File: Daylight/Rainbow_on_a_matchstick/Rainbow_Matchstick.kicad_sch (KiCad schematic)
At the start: 22 parts, among them J1 Conn_01x03_Male, J2 Conn_01x01_Male, J3 Conn_01x01_Male

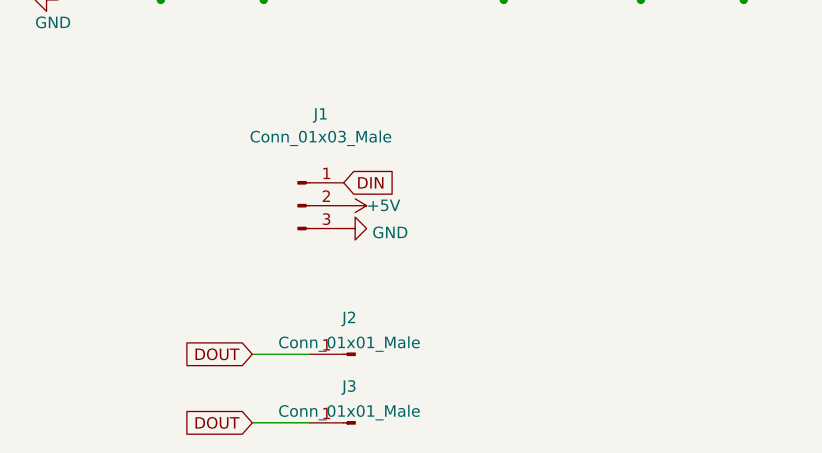
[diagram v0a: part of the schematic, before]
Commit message: Daylight | Add output connectors to the RGB sticks
Provided pick and place files for all varieties as well.
Created individual README.md files with BOM and changelog.
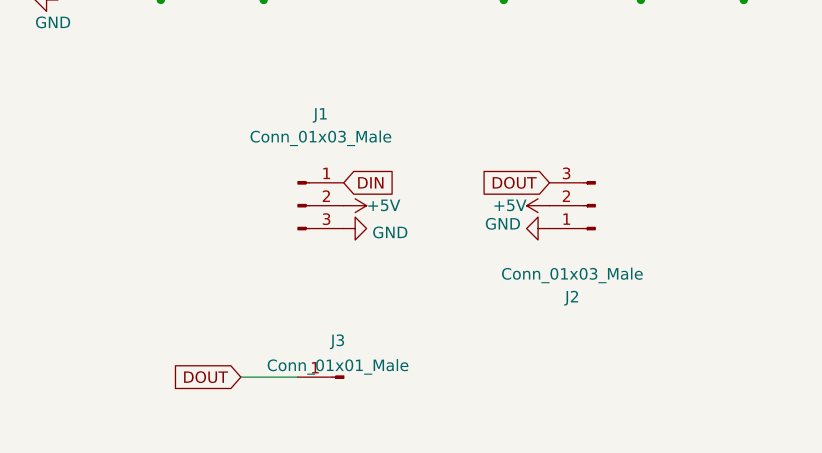
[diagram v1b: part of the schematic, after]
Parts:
- removed J2: Conn_01x01_Male, Daylight:PinHeader-1-with-SMDpad, symbol Connector:Conn_01x01_Male
- added J2: Conn_01x03_Male, Daylight:JST_XH_S3B-XH-A-1_1x03_P2.50mm_Horizontal, symbol Connector:Conn_01x03_Male
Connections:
- net +5V: now also J2.2 (Pin_2)
- net DOUT: now also J2.3 (Pin_3)
- net GND: now also J2.1 (Pin_1)
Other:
- moved on the sheet: J3
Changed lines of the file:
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@@
-    (stroke (width 0) (type default) (color 0 0 0 0))
-  )
-  (wire (pts (xy 48.26 105.41) (xy 54.61 105.41))
     (stroke (width 0) (type default) (color 0 0 0 0))
   )
@@
     (stroke (width 0) (type default) (color 0 0 0 0))
   )
-  (wire (pts (xy 48.26 113.03) (xy 54.61 113.03))
+  (wire (pts (xy 46.99 107.95) (xy 53.34 107.95))
     (stroke (width 0) (type default) (color 0 0 0 0))
   )
@@
     )
   )
+  (global_label "DOUT" (shape input) (at 81.28 86.36 180) (fields_autoplaced)
+    (effects (font (size 1.27 1.27)) (justify right))
+    (property "Intersheet References" "${INTERSHEET_REFS}" (id 0) (at 73.9683 86.2806 0)
+      (effects (font (size 1.27 1.27)) (justify right) hide)
+    )
+  )
   (global_label "DIN" (shape input) (at 26.67 35.56 180) (fields_autoplaced)
     (effects (font (size 1.27 1.27)) (justify right))
@@
     )
   )
-  (global_label "DOUT" (shape input) (at 48.26 113.03 180) (fields_autoplaced)
+  (global_label "DOUT" (shape input) (at 46.99 107.95 180) (fields_autoplaced)
     (effects (font (size 1.27 1.27)) (justify right))
-    (property "Intersheet References" "${INTERSHEET_REFS}" (id 0) (at 40.9483 112.9506 0)
-      (effects (font (size 1.27 1.27)) (justify right) hide)
-    )
-  )
-  (global_label "DOUT" (shape input) (at 48.26 105.41 180) (fields_autoplaced)
-    (effects (font (size 1.27 1.27)) (justify right))
-    (property "Intersheet References" "${INTERSHEET_REFS}" (id 0) (at 40.9483 105.3306 0)
+    (property "Intersheet References" "${INTERSHEET_REFS}" (id 0) (at 39.6783 107.8706 0)
       (effects (font (size 1.27 1.27)) (justify right) hide)
     )
@@
   (symbol (lib_id "power:GND") (at 58.42 91.44 90) (unit 1)
     (in_bom yes) (on_board yes) (fields_autoplaced)
-    (property "Reference" "#PWR08" (id 0) (at 64.77 91.44 0)
+    (property "Reference" "#PWR09" (id 0) (at 64.77 91.44 0)
       (effects (font (size 1.27 1.27)) hide)
     )
@@
     (pin "4")
   )
-  (symbol (lib_id "Connector:Conn_01x01_Male") (at 59.69 105.41 180) (unit 1)
-    (in_bom yes) (on_board yes) (fields_autoplaced)
-    (property "Reference" "J2" (id 0) (at 59.055 101.3673 0))
-    (property "Value" "Conn_01x01_Male" (id 1) (at 59.055 104.1424 0))
-    (property "Footprint" "Daylight:PinHeader-1-with-SMDpad" (id 2) (at 59.69 105.41 0)
-      (effects (font (size 1.27 1.27)) hide)
-    )
-    (property "Datasheet" "~" (id 3) (at 59.69 105.41 0)
-      (effects (font (size 1.27 1.27)) hide)
-    )
-    (pin "1")
-  )
   (symbol (lib_id "LED:WS2812B") (at 156.21 35.56 0) (unit 1)
     (in_bom yes) (on_board yes)
@@
     (pin "4")
   )
-  (symbol (lib_id "Connector:Conn_01x01_Male") (at 59.69 113.03 180) (unit 1)
-    (in_bom yes) (on_board yes) (fields_autoplaced)
-    (property "Reference" "J3" (id 0) (at 59.055 108.9873 0))
-    (property "Value" "Conn_01x01_Male" (id 1) (at 59.055 111.7624 0))
-    (property "Footprint" "Daylight:PinHeader-1-with-SMDpad" (id 2) (at 59.69 113.03 0)
-      (effects (font (size 1.27 1.27)) hide)
-    )
-    (property "Datasheet" "~" (id 3) (at 59.69 113.03 0)
+  (symbol (lib_id "Connector:Conn_01x01_Male") (at 58.42 107.95 180) (unit 1)
+    (in_bom yes) (on_board yes) (fields_autoplaced)
+    (property "Reference" "J3" (id 0) (at 57.785 103.9073 0))
+    (property "Value" "Conn_01x01_Male" (id 1) (at 57.785 106.6824 0))
+    (property "Footprint" "Daylight:PinHeader-1-with-SMDpad" (id 2) (at 58.42 107.95 0)
+      (effects (font (size 1.27 1.27)) hide)
+    )
+    (property "Datasheet" "~" (id 3) (at 58.42 107.95 0)
       (effects (font (size 1.27 1.27)) hide)
     )
@@
     (pin "1")
     (pin "2")
+  )
+  (symbol (lib_id "Connector:Conn_01x03_Male") (at 86.36 88.9 180) (unit 1)
+    (in_bom yes) (on_board yes)
+    (property "Reference" "J2" (id 0) (at 83.82 99.06 0))
+    (property "Value" "Conn_01x03_Male" (id 1) (at 83.82 96.52 0))
+    (property "Footprint" "Daylight:JST_XH_S3B-XH-A-1_1x03_P2.50mm_Horizontal" (id 2) (at 86.36 88.9 0)
+      (effects (font (size 1.27 1.27)) hide)
+    )
+    (property "Datasheet" "~" (id 3) (at 86.36 88.9 0)
+      (effects (font (size 1.27 1.27)) hide)
+    )
+    (pin "1")
+    (pin "2")
+    (pin "3")
   )
   (symbol (lib_id "Device:C_Small") (at 171.45 35.56 0) (mirror x) (unit 1)
@@
     (pin "4")
   )
+  (symbol (lib_id "power:+5V") (at 81.28 88.9 90) (unit 1)
+    (in_bom yes) (on_board yes)
+    (property "Reference" "#PWR08" (id 0) (at 85.09 88.9 0)
+      (effects (font (size 1.27 1.27)) hide)
+    )
+    (property "Value" "+5V" (id 1) (at 78.74 88.9 90)
+      (effects (font (size 1.27 1.27)) (justify left))
+    )
+    (property "Footprint" "" (id 2) (at 81.28 88.9 0)
+      (effects (font (size 1.27 1.27)) hide)
+    )
+    (property "Datasheet" "" (id 3) (at 81.28 88.9 0)
+      (effects (font (size 1.27 1.27)) hide)
+    )
+    (pin "1")
+  )
   (symbol (lib_id "Device:C_Small") (at 144.78 35.56 0) (mirror x) (unit 1)
     (in_bom yes) (on_board yes) (fields_autoplaced)
@@
     (pin "1")
   )
+  (symbol (lib_id "power:GND") (at 81.28 91.44 270) (unit 1)
+    (in_bom yes) (on_board yes) (fields_autoplaced)
+    (property "Reference" "#PWR010" (id 0) (at 74.93 91.44 0)
+      (effects (font (size 1.27 1.27)) hide)
+    )
+    (property "Value" "GND" (id 1) (at 78.105 90.961 90)
+      (effects (font (size 1.27 1.27)) (justify right))
+    )
+    (property "Footprint" "" (id 2) (at 81.28 91.44 0)
+      (effects (font (size 1.27 1.27)) hide)
+    )
+    (property "Datasheet" "" (id 3) (at 81.28 91.44 0)
+      (effects (font (size 1.27 1.27)) hide)
+    )
+    (pin "1")
+  )
   (sheet_instances
     (path "/" (page "1"))
@@
       (reference "#PWR07") (unit 1) (value "+5V") (footprint "")
     )
+    (path "/9d48d597-b34c-4d62-95c8-00458414359f"
+      (reference "#PWR08") (unit 1) (value "+5V") (footprint "")
+    )
     (path "/15200114-c51a-4499-97e2-8f516170757e"
-      (reference "#PWR08") (unit 1) (value "GND") (footprint "")
+      (reference "#PWR09") (unit 1) (value "GND") (footprint "")
+    )
+    (path "/fed927fe-eafb-4471-ac5d-756725ea174d"
+      (reference "#PWR010") (unit 1) (value "GND") (footprint "")
     )
     (path "/68e93e90-6c9f-4df4-a152-689b3093e61f"
@@
       (reference "J1") (unit 1) (value "Conn_01x03_Male") (footprint "Daylight:JST_XH_S3B-XH-A-1_1x03_P2.50mm_Horizontal")
     )
-    (path "/605257da-4003-49fc-aabc-f508bd369671"
-      (reference "J2") (unit 1) (value "Conn_01x01_Male") (footprint "Daylight:PinHeader-1-with-SMDpad")
+    (path "/77f01482-1a0d-408c-a0b8-f389b6fedc82"
+      (reference "J2") (unit 1) (value "Conn_01x03_Male") (footprint "Daylight:JST_XH_S3B-XH-A-1_1x03_P2.50mm_Horizontal")
     )
     (path "/627442c6-bd82-4a5c-a454-79108c16ffc2"
